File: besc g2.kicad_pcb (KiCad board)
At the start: 4 copper layers, 231 x 67 mm, 300 parts, among them IC1 LTC7801, J1 PHASE WIRE, J10 614105150721, J11 THROTTLE, J12 MOTOR SENSOR, J13 THROTTLE 2 (BRAKE), J14 SERIAL, J15 IGNITION, J16 CAN, J17 12V OUT, J2 PHASE WIRE, J3 PHASE WIRE, J4 BUSBAR, J5 BUSBAR, J6 IN+, J7 IN-, J8 SWD, J9 RC PWM, Q1 IRF135B203, Q10 IRF135B203, Q11 IRF135B203, Q12 IRF135B203, Q13 IRF135B203, Q14 IRF135B203, Q15 IRF135B203, Q16 IRF135B203, Q17 IRF135B203, Q18 IRF135B203, Q19 IRF135B203, Q2 IRF135B203, Q20 IRF135B203, Q21 IRF135B203, Q22 IRF135B203, Q23 IRF135B203, Q24 IRF135B203, Q25 FDMS86252L, Q26 BSC110N15NS5, Q3 IRF135B203, Q4 IRF135B203, Q5 IRF135B203, Q6 IRF135B203, Q7 IRF135B203, Q8 IRF135B203, Q9 IRF135B203, U1 UCC21520DW, U10 TJA1051T-3, U11 R-78E5.0-0.5, U12 LP5907MFX-3.3, U2 UCC21520DW, U3 UCC21520DW, U4 INA240A1D, U5 INA240A1D, U6 INA240A1D, U8 STM32F405RGTx, U9 USBLC6-2SC6, Y1 MCSJK-7I-8.00-18-10-60-B-10

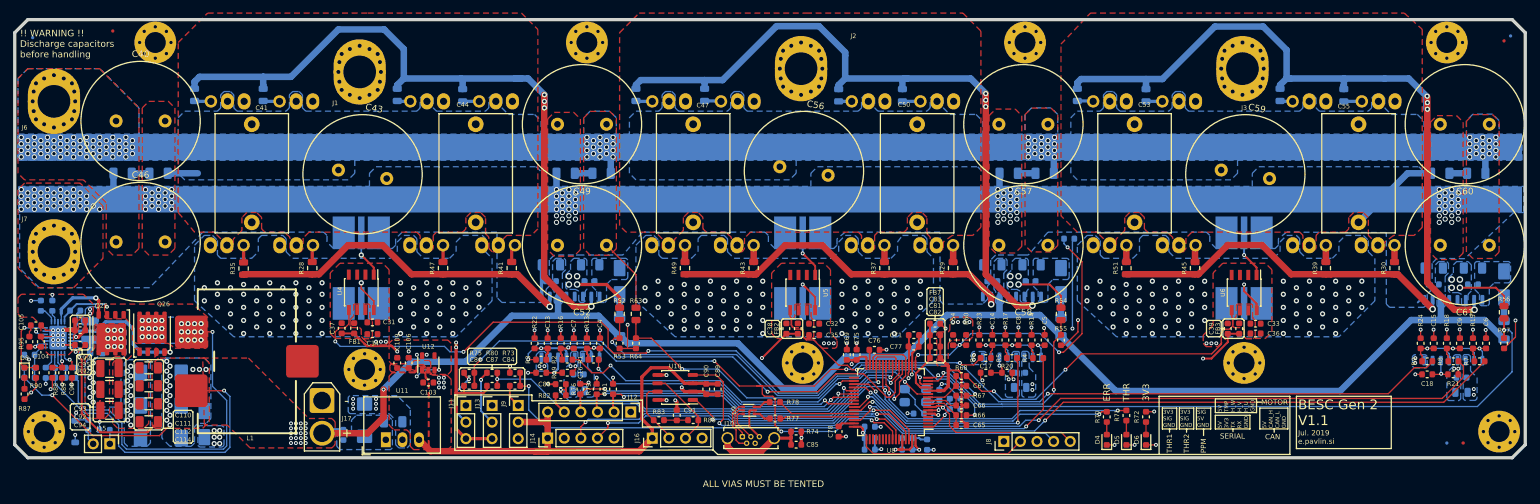
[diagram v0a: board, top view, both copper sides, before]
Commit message: Added brakes, i2c
Signed-off-by: manianac <manianac@gmail.com>
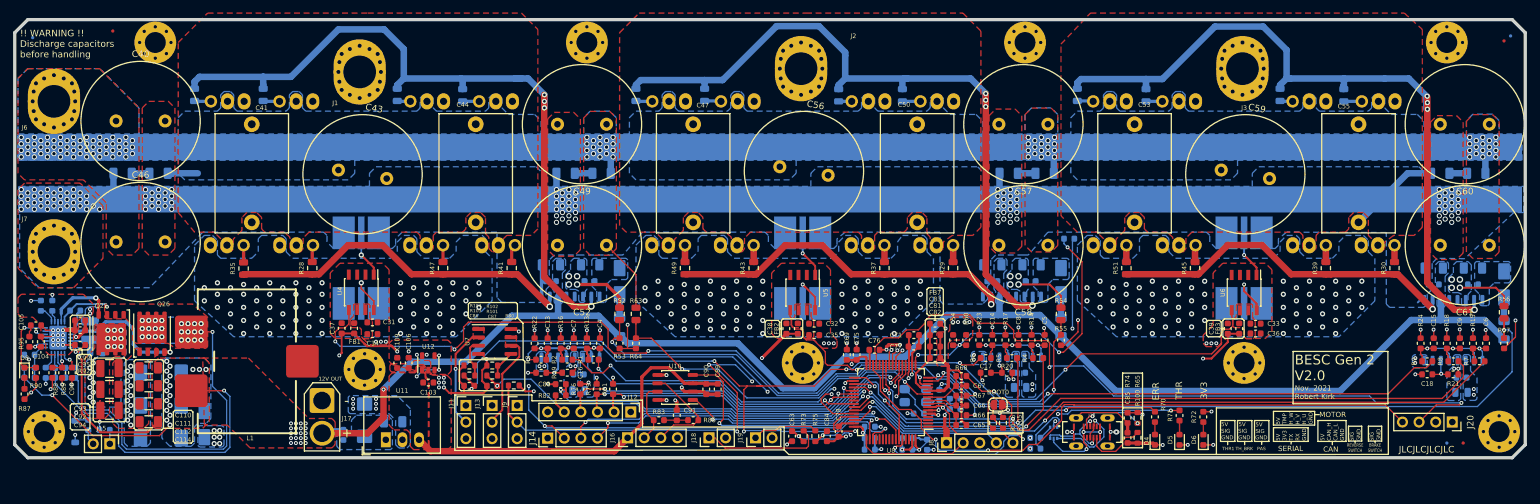
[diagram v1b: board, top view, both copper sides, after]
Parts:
- added C63: 100n, Capacitor_SMD:C_0603_1608Metric, F.Cu at (150.7, 124.6)
- added J18: BRAKE_SW, Connector_PinHeader_2.54mm:PinHeader_1x02_P2.54mm_Vertical, F.Cu at (138.0, 124.9)
- added J19: REVERSE_SW, Connector_PinHeader_2.54mm:PinHeader_1x02_P2.54mm_Vertical, F.Cu at (145.1, 124.9)
- added J20: I2C, Connector_PinSocket_2.54mm:PinSocket_1x04_P2.54mm_Vertical, F.Cu at (251.6, 122.4)
- added JP2: BOOT0, Jumper:SolderJumper-2_P1.3mm_Open_RoundedPad1.0x1.5mm, F.Cu at (182.2, 119.8)
- added R100: 5K1, Resistor_SMD:R_0603_1608Metric, F.Cu at (203.5, 124.9)
- added R101: 1k8, Resistor_SMD:R_0603_1608Metric, F.Cu at (104.8, 115.3)
- added R102: 3k3, Resistor_SMD:R_0603_1608Metric, F.Cu at (104.8, 113.8)
- added R103: 1k8, Resistor_SMD:R_0603_1608Metric, F.Cu at (101.3, 115.3)
- added R104: 3k3, Resistor_SMD:R_0603_1608Metric, F.Cu at (101.3, 113.8)
- added R105: 2k2, Resistor_SMD:R_0603_1608Metric, F.Cu at (182.9, 122.6)
- added R106: 10k, Resistor_SMD:R_0603_1608Metric, F.Cu at (181.4, 122.6)
- added R65: 5K1, Resistor_SMD:R_0603_1608Metric, F.Cu at (203.5, 121.8)
- added U7: LMV358, Package_SO:SOIC-8_3.9x4.9mm_P1.27mm, F.Cu at (105.2, 110.1)
- C40, C43, C46, C49, C52, C56, C57, C58, C59, C60, C61: footprint moje:C_Radial_D18.0mm_H25mm_P7.50mm -> Capacitor_THT:C_Radial_D18.0mm_H35.5mm_P7.50mm
- J10: value 614105150721 -> USB_C_Receptacle_USB2.0; footprint Connector_USB:USB_Micro-B_Wuerth_614105150721_Vertical_CircularHoles -> BESC-G2:GCT_USB4120-03-C_REVA
- J14: footprint Connector_PinHeader_2.54mm:PinHeader_1x05_P2.54mm_Vertical -> Connector_PinHeader_2.54mm:PinHeader_1x04_P2.54mm_Vertical
- J9: value RC PWM -> PAS
- R77, R78, U9: moved to B.Cu
- moved R75 53.8 mm to (154.2, 124.6), turned to 90 degrees
- moved J10 53.4 mm to (196.5, 124.0)
- moved R74 50.7 mm to (202.0, 121.8), turned to 270 degrees
- moved C85 50.7 mm to (202.0, 124.9), turned to 270 degrees
- moved C84 48.7 mm to (156.0, 124.6), turned to 270 degrees
- moved U9 46.8 mm to (190.7, 124.1), turned to 270 degrees
- moved R73 44.8 mm to (152.4, 124.6), turned to 90 degrees
- moved R78 40.5 mm to (187.9, 126.5), turned to 180 degrees
- moved R77 39.9 mm to (187.9, 124.9), turned to 180 degrees
- moved D6 8.76 mm to (213.6, 125.2)
- moved R72 8.76 mm to (213.6, 121.7)
- moved J8 8.76 mm to (174.3, 125.6)
- moved D5 8.13 mm to (209.9, 125.2)
- moved R71 8.13 mm to (209.9, 121.4)
- moved D4 7.37 mm to (206.2, 125.2)
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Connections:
- C84 pad 1: /io/RC_PWM -> /io/REVERSE_SW
- C86 pad 1: /mcu/SCK_ADC_EXT -> /mcu/ADC_THROTTLE
- C87 pad 1: /mcu/MISO_ADC_EXT2 -> /mcu/ADC_THBRAKE
- J11 pad 1: +3V3 -> +5V
- J13 pad 1: +3V3 -> +5V
- J14 pad 1: +5V -> +3V3
- J14 pad 2: +3V3 -> /io/UART_TX
- J14 pad 3: /io/TX -> /io/UART_RX
- J14 pad 4: /io/RX -> GND
- J9 pad 1: Net-(J9-Pad1) -> +5V
- J9 pad 2: +5V -> /mcu/HALL_PAS
- R3 pad 2: /mcu/DISABLE -> /mcu/GATE_DISABLE
- R6 pad 2: /mcu/DISABLE -> /mcu/GATE_DISABLE
- R73 pad 1: Net-(J9-Pad1) -> /io/BRAKE_SW
- R73 pad 2: /io/RC_PWM -> Net-(J18-Pad1)
- R75 pad 1: Net-(J11-Pad2) -> /io/REVERSE_SW
- R75 pad 2: /mcu/SCK_ADC_EXT -> Net-(J19-Pad1)
- R80 pad 1: Net-(J13-Pad2) -> /mcu/HALL_PAS
- R80 pad 2: /mcu/MISO_ADC_EXT2 -> +3V3
- R9 pad 2: /mcu/DISABLE -> /mcu/GATE_DISABLE
- U1 pad 12: (no net) -> Net-(U1-Pad12)
- U1 pad 13: (no net) -> Net-(U1-Pad13)
- U1 pad 7: (no net) -> Net-(U1-Pad7)
- U12 pad 4: +3V3 -> GND
- U2 pad 12: (no net) -> Net-(U2-Pad12)
- U2 pad 13: (no net) -> Net-(U2-Pad13)
- U2 pad 7: (no net) -> Net-(U2-Pad7)
- U3 pad 12: (no net) -> Net-(U3-Pad12)
- U3 pad 13: (no net) -> Net-(U3-Pad13)
- U3 pad 7: (no net) -> Net-(U3-Pad7)
- U8 pad 2: (no net) -> Net-(U8-Pad2)
- U8 pad 20: /io/RX -> /io/MOTOR_TEMP
- U8 pad 21: /mcu/SCK_ADC_EXT -> /mcu/ADC_THROTTLE
- U8 pad 22: /mcu/MISO_ADC_EXT2 -> /mcu/ADC_THBRAKE
- U8 pad 23: /io/TX -> /mcu/PWM_U_LOW
- U8 pad 24: /io/MOTOR_TEMP -> /mcu/HALL_PAS
- U8 pad 25: (no net) -> /io/BRAKE_SW
- U8 pad 26: Net-(R71-Pad2) -> /mcu/PWM_V_LOW
- U8 pad 27: Net-(R70-Pad2) -> /mcu/PWM_W_LOW
- U8 pad 28: (no net) -> /mcu/FAULT
- U8 pad 29: /io/TX -> /io/I2C_SCL
- U8 pad 3: (no net) -> Net-(U8-Pad3)
- U8 pad 30: /io/RX -> /io/I2C_SDA
- U8 pad 33: (no net) -> /io/CAN_RX
- U8 pad 34: /mcu/PWM_U_LOW -> /io/CAN_TX
- U8 pad 35: /mcu/PWM_V_LOW -> Net-(R71-Pad2)
- U8 pad 36: /mcu/PWM_W_LOW -> Net-(R70-Pad2)
- U8 pad 4: (no net) -> Net-(U8-Pad4)
- U8 pad 40: (no net) -> Net-(U8-Pad40)
- U8 pad 50: (no net) -> /mcu/GATE_DISABLE
- U8 pad 51: (no net) -> /io/REVERSE_SW
- U8 pad 52: (no net) -> Net-(U8-Pad52)
- U8 pad 53: (no net) -> Net-(U8-Pad53)
- U8 pad 54: (no net) -> Net-(U8-Pad54)
- U8 pad 55: (no net) -> /mcu/SPI_SCK
- U8 pad 56: (no net) -> /mcu/SPI_MISO
- U8 pad 57: /mcu/DISABLE -> /mcu/SPI_MOSI
- U8 pad 58: /io/RC_PWM -> /io/UART_TX
- U8 pad 59: (no net) -> /io/UART_RX
- U8 pad 60: GND -> Net-(R106-Pad2)
- U8 pad 61: /io/CAN_RX -> Net-(U8-Pad61)
- U8 pad 62: /io/CAN_TX -> Net-(U8-Pad62)
- U9 pad 4: Net-(J10-Pad2) -> Net-(J10-PadA7)
- U9 pad 5: Net-(J10-Pad1) -> Net-(J10-PadA4)
- U9 pad 6: Net-(J10-Pad3) -> Net-(J10-PadA6)
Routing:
- net /mcu/GATE_DISABLE: track 0.00 -> 185.5 mm, vias 0 -> 7
- net /mcu/DISABLE: track 183.5 -> 0.00 mm, vias 7 -> 0
- net /io/I2C_SCL: track 0.00 -> 111.0 mm, vias 0 -> 2
- net /io/I2C_SDA: track 0.00 -> 94.5 mm, vias 0 -> 2
- net /mcu/HALL_PAS: track 0.00 -> 91.7 mm, vias 0 -> 4
- net /mcu/ADC_THROTTLE: track 0.00 -> 82.6 mm, vias 0 -> 3
- net /mcu/SCK_ADC_EXT: track 79.8 -> 0.00 mm, vias 2 -> 0
- net /mcu/ADC_THBRAKE: track 0.00 -> 71.2 mm, vias 0 -> 2
- net /mcu/MISO_ADC_EXT2: track 70.5 -> 0.00 mm, vias 2 -> 0
- net /io/UART_TX: track 0.00 -> 67.7 mm, vias 0 -> 3
- net /io/RC_PWM: track 67.3 -> 0.00 mm, vias 2 -> 0
- net /io/RX: track 64.6 -> 0.00 mm, vias 2 -> 0
- net /io/UART_RX: track 0.00 -> 62.0 mm, vias 0 -> 2
- net /io/TX: track 58.7 -> 0.00 mm, vias 2 -> 0
- net GND: track 207.6 -> 253.1 mm, vias 241 -> 248
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- added copper zone on In1.Cu, net +5V
- added copper zone on F.Cu, net Net-(J11-Pad2)
- added copper zone on F.Cu, net Net-(J13-Pad2)
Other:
- board text added: "BESC Gen 2 V2.0"
- board text added: "BRAKE SWITCH"
- board text added: "JLCJLCJLCJLC"
- board text added: "Nov. 2021 Robert Kirk"
- board text added: "PAS"
- board text added: "REVERSE SWITCH"
- board text added: "TH_BRK"
- board text removed: "ALL VIAS MUST BE TENTED"
- board text removed: "BESC Gen 2 V1.1"
- board text removed: "Jul. 2019 e.pavlin.si"
- board text removed: "PPM"
- board text removed: "THR2"
